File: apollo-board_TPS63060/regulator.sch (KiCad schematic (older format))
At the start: 44 parts, among them J11 Conn_01x04_Male, Q10 2N7002A, Q11 2N7002A, Q13 DMP2035UVT, Q14 DMP2035UVT, Q5 DMP2035UVT, Q9 2N7002A, U10 TPS63060, U9 TPS63060

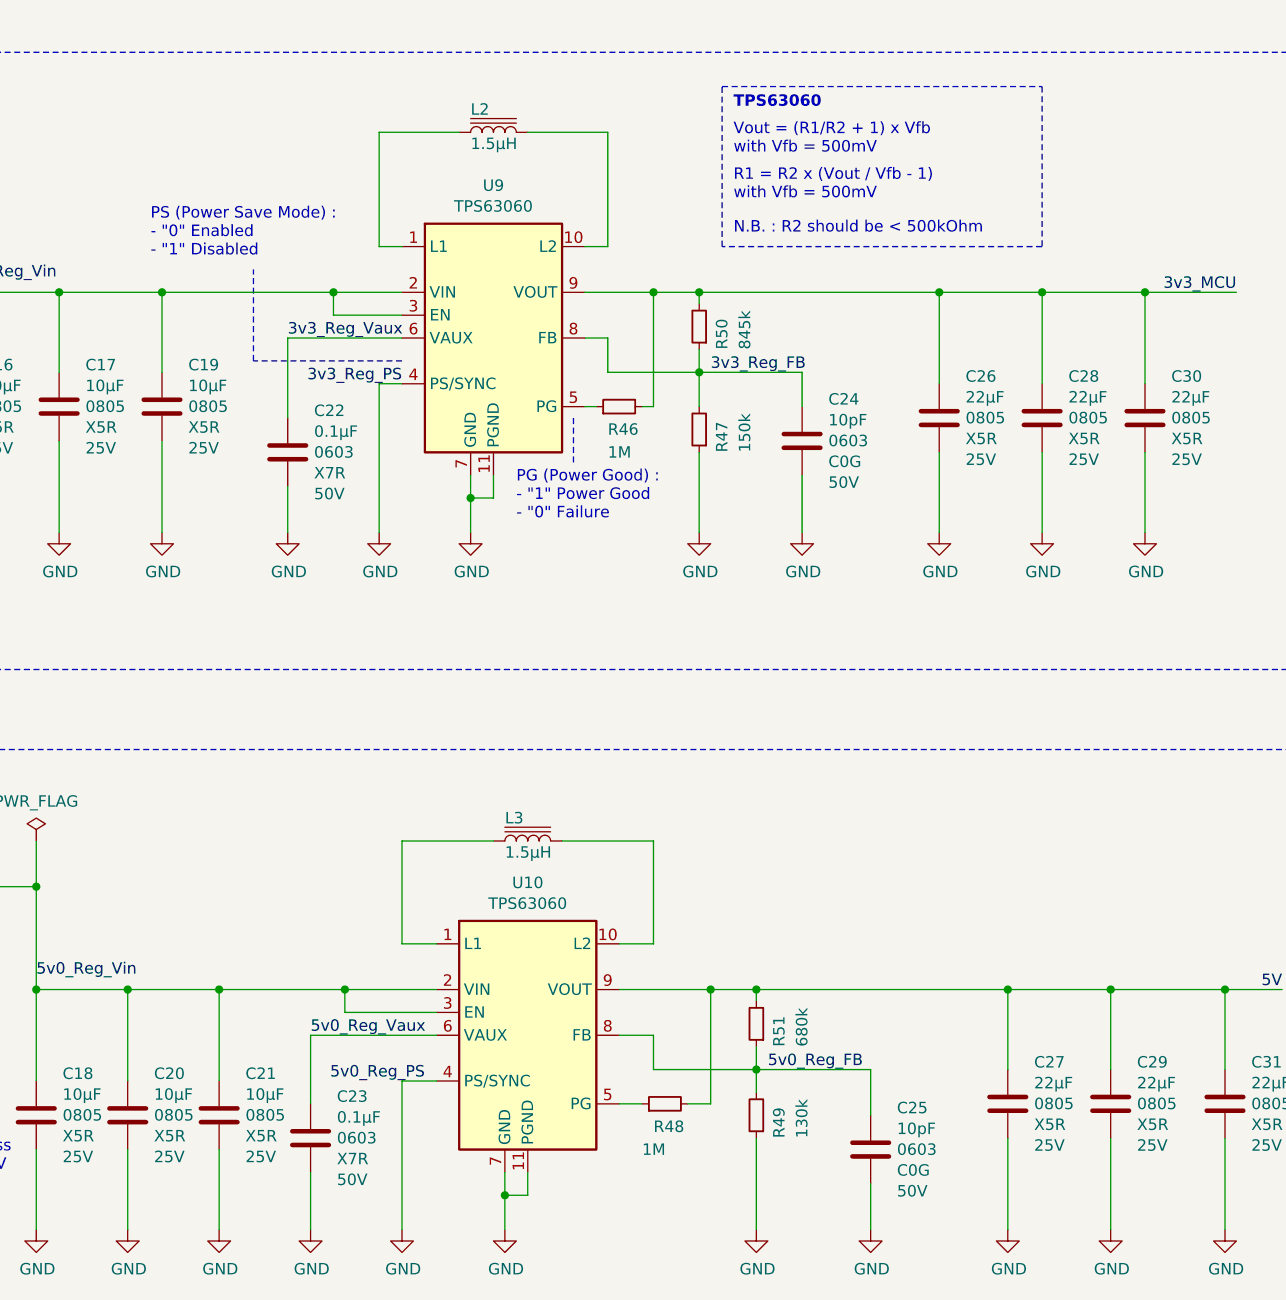
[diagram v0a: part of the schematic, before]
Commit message: Update +5V Buck-Boost Feedback resistor values
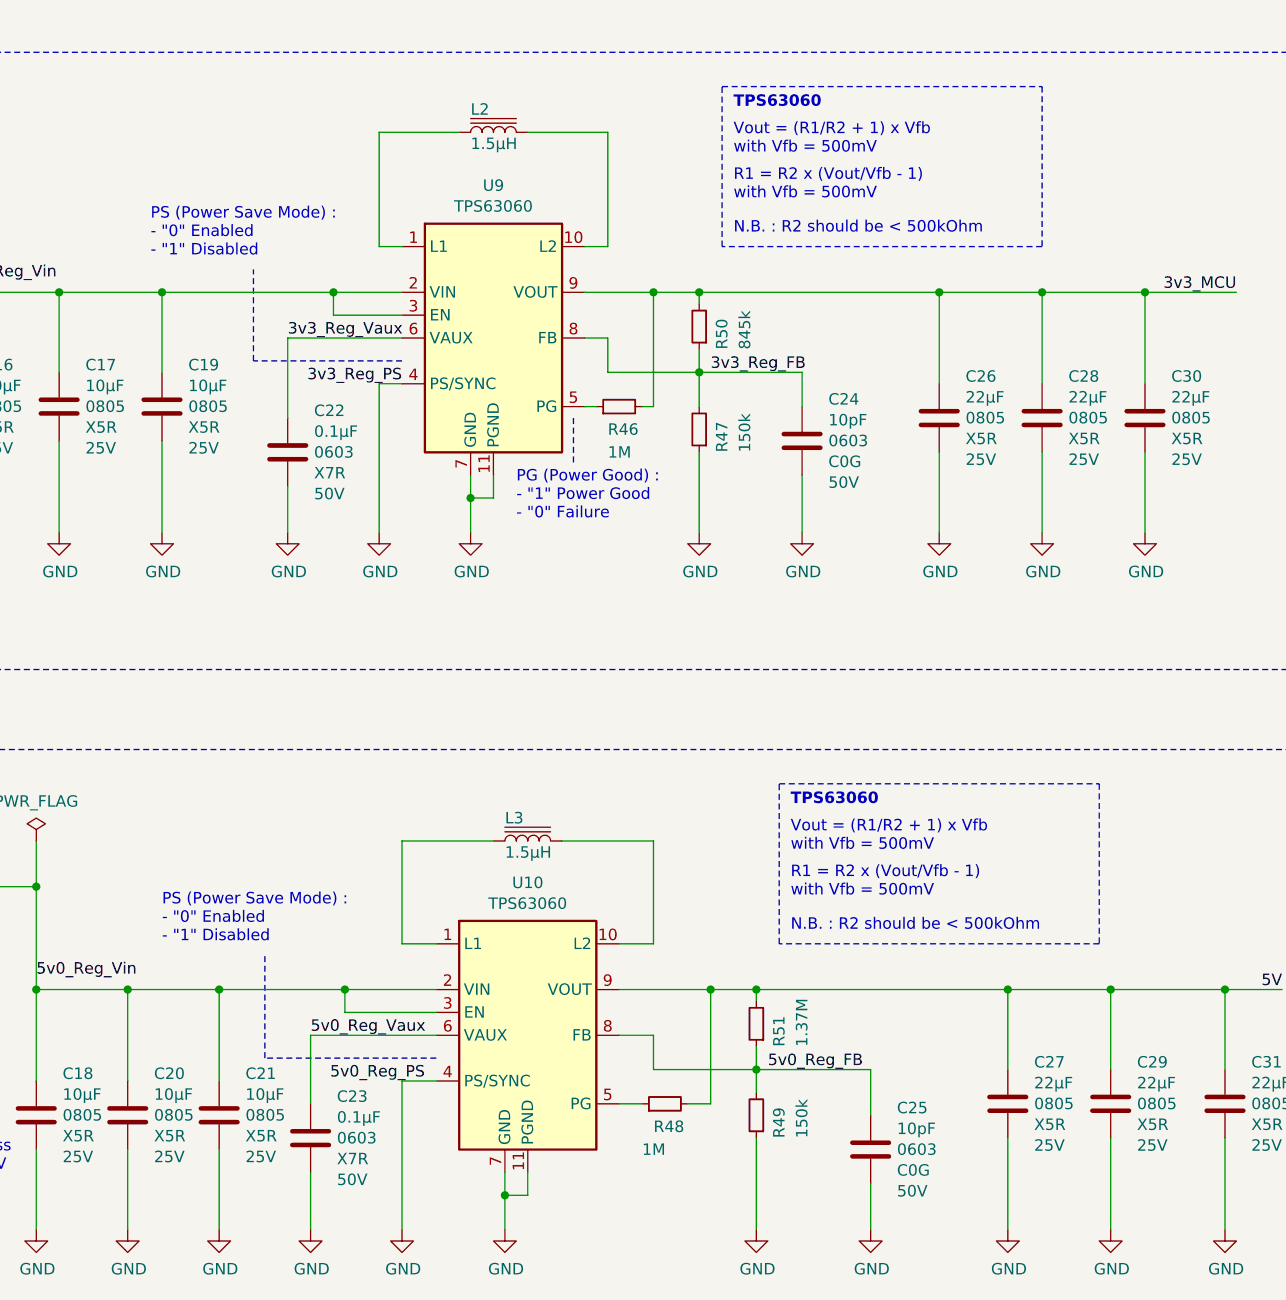
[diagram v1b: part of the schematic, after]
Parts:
- R49: value 130k -> 150k
- R51: value 680k -> 1.37M
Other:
- note added: "R1 = R2 x (Vout/Vfb - 1)\nwith Vfb = 500mV"
- note removed: "R1 = R2 x (Vout / Vfb - 1)\nwith Vfb = 500mV"
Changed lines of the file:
@@
 P 8400 5350
 F 0 "R49" V 8300 5450 50  0000 R CNN
-F 1 "130k" V 8200 5450 50  0000 R CNN
+F 1 "150k" V 8200 5450 50  0000 R CNN
 F 2 "Resistor_SMD:R_0603_1608Metric" H 8400 5350 50  0001 C CNN
 F 3 "~" H 8400 5350 50  0001 C CNN
@@
 P 8400 4950
 F 0 "R51" V 8300 5050 50  0000 R CNN
-F 1 "680k" V 8200 5050 50  0000 R CNN
+F 1 "1.37M" V 8200 5050 50  0000 R CNN
 F 2 "Resistor_SMD:R_0603_1608Metric" H 8400 4950 50  0001 C CNN
 F 3 "~" H 8400 4950 50  0001 C CNN
@@
 N.B. : R2 should be < 500kOhm
 Text Notes 8300 1350 0    50   ~ 0
-R1 = R2 x (Vout / Vfb - 1)\nwith Vfb = 500mV
+R1 = R2 x (Vout/Vfb - 1)\nwith Vfb = 500mV
 Wire Notes Line
 	6850 2050 6200 2050
@@
 Wire Wire Line
 	5250 4800 5250 5200
+Text Notes 8550 4200 0    50   ~ 0
+Vout = (R1/R2 + 1) x Vfb\nwith Vfb = 500mV
+Text Notes 8550 4550 0    50   ~ 0
+N.B. : R2 should be < 500kOhm
+Text Notes 8550 4400 0    50   ~ 0
+R1 = R2 x (Vout/Vfb - 1)\nwith Vfb = 500mV
+Text Notes 8550 4000 0    50   ~ 10
+TPS63060
+Wire Notes Line
+	8500 3900 9900 3900
+Wire Notes Line
+	9900 3900 9900 4600
+Wire Notes Line
+	9900 4600 8500 4600
+Wire Notes Line
+	8500 4600 8500 3900
+Text Notes 5800 4600 0    50   ~ 0
+PS (Power Save Mode) :\n- "0" Enabled\n- "1" Disabled
+Wire Notes Line
+	6250 5100 6250 4650
+Wire Notes Line
+	7000 5100 6250 5100
 $EndSCHEMATC

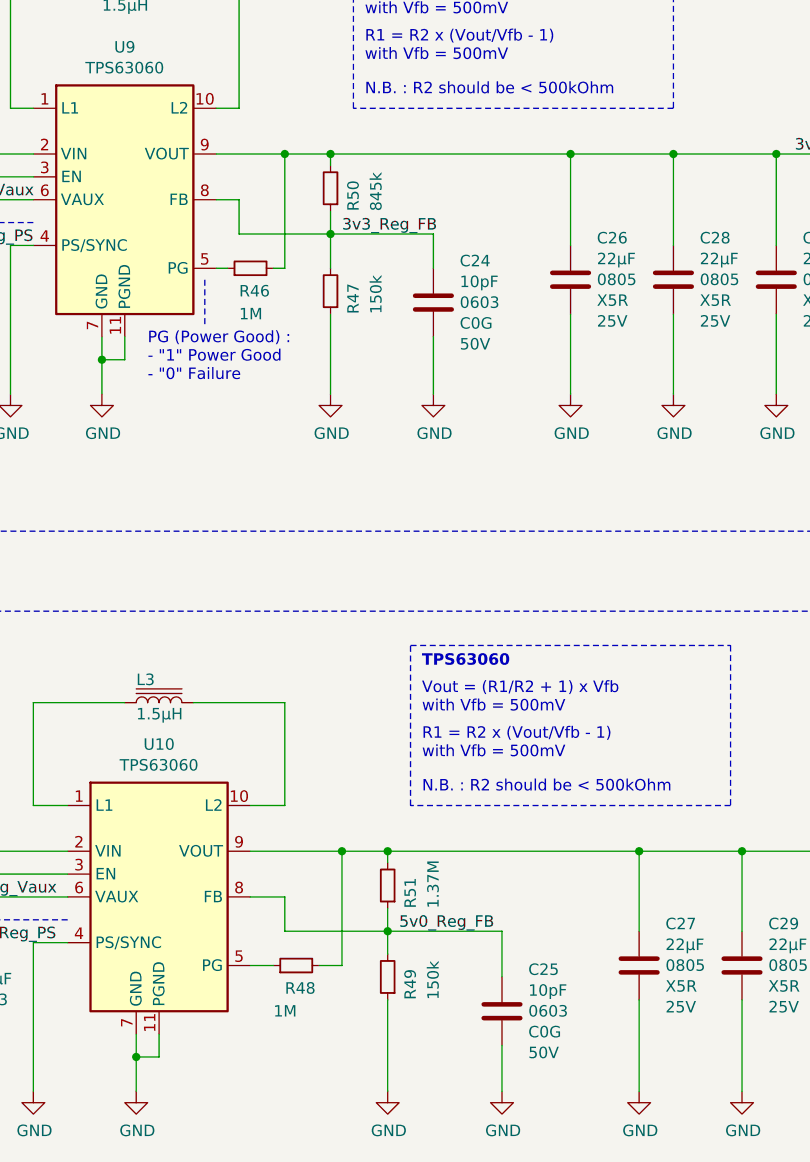
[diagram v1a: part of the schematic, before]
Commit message: Update Buck-Boost Feedback Resistor values
- Use common values + bridge divider iq >3µA
- Misc. Routing : increase one track width from 0.25 to 0.28mm (+5V Output)
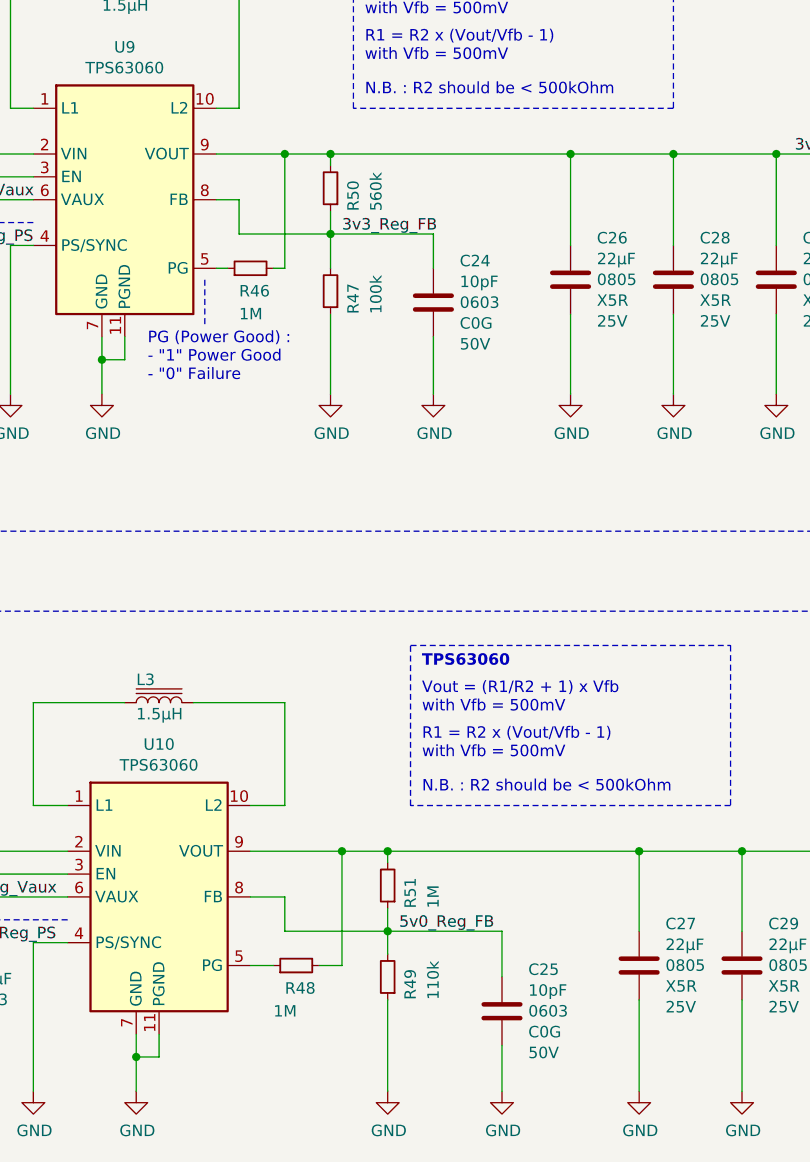
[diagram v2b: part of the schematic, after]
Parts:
- R47: value 150k -> 100k
- R49: value 150k -> 110k
- R50: value 845k -> 560k
- R51: value 1.37M -> 1M
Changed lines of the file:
@@
 P 8400 5350
 F 0 "R49" V 8300 5450 50  0000 R CNN
-F 1 "150k" V 8200 5450 50  0000 R CNN
+F 1 "110k" V 8200 5450 50  0000 R CNN
 F 2 "Resistor_SMD:R_0603_1608Metric" H 8400 5350 50  0001 C CNN
 F 3 "~" H 8400 5350 50  0001 C CNN
@@
 P 8400 4950
 F 0 "R51" V 8300 5050 50  0000 R CNN
-F 1 "1.37M" V 8200 5050 50  0000 R CNN
+F 1 "1M" V 8200 5050 50  0000 R CNN
 F 2 "Resistor_SMD:R_0603_1608Metric" H 8400 4950 50  0001 C CNN
 F 3 "~" H 8400 4950 50  0001 C CNN
@@
 P 8150 1900
 F 0 "R50" V 8050 2000 50  0000 R CNN
-F 1 "845k" V 7950 2000 50  0000 R CNN
+F 1 "560k" V 7950 2000 50  0000 R CNN
 F 2 "Resistor_SMD:R_0603_1608Metric" H 8150 1900 50  0001 C CNN
 F 3 "~" H 8150 1900 50  0001 C CNN
@@
 P 8150 2350
 F 0 "R47" V 8050 2450 50  0000 R CNN
-F 1 "150k" V 7950 2450 50  0000 R CNN
+F 1 "100k" V 7950 2450 50  0000 R CNN
 F 2 "Resistor_SMD:R_0603_1608Metric" H 8150 2350 50  0001 C CNN
 F 3 "~" H 8150 2350 50  0001 C CNN

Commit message: Update USB-C receptacle symbol fields
Add Mfr Name & ref., DataSheet + Alternative Equivalent Part
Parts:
- U10, U9: footprint TPS63060:Texas_S-PWSON-N10_ThermalVias -> TPS63060:Texas_S-PWSON-N10_ThermalVias_NSM_vias_bottom
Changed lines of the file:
@@
 F 0 "U9" H 7250 2617 50  0000 C CNN
 F 1 "TPS63060" H 7250 2526 50  0000 C CNN
-F 2 "TPS63060:Texas_S-PWSON-N10_ThermalVias" H 7250 1300 50  0001 C CNN
+F 2 "TPS63060:Texas_S-PWSON-N10_ThermalVias_NSM_vias_bottom" H 7250 1300 50  0001 C CNN
 F 3 "http://www.ti.com/lit/ds/symlink/tps63060.pdf" H 7250 1950 50  0001 C CNN
 	1    7250 1950
@@
 F 0 "U10" H 7400 5667 50  0000 C CNN
 F 1 "TPS63060" H 7400 5576 50  0000 C CNN
-F 2 "TPS63060:Texas_S-PWSON-N10_ThermalVias" H 7400 4350 50  0001 C CNN
+F 2 "TPS63060:Texas_S-PWSON-N10_ThermalVias_NSM_vias_bottom" H 7400 4350 50  0001 C CNN
 F 3 "http://www.ti.com/lit/ds/symlink/tps63060.pdf" H 7400 5000 50  0001 C CNN
 	1    7400 5000

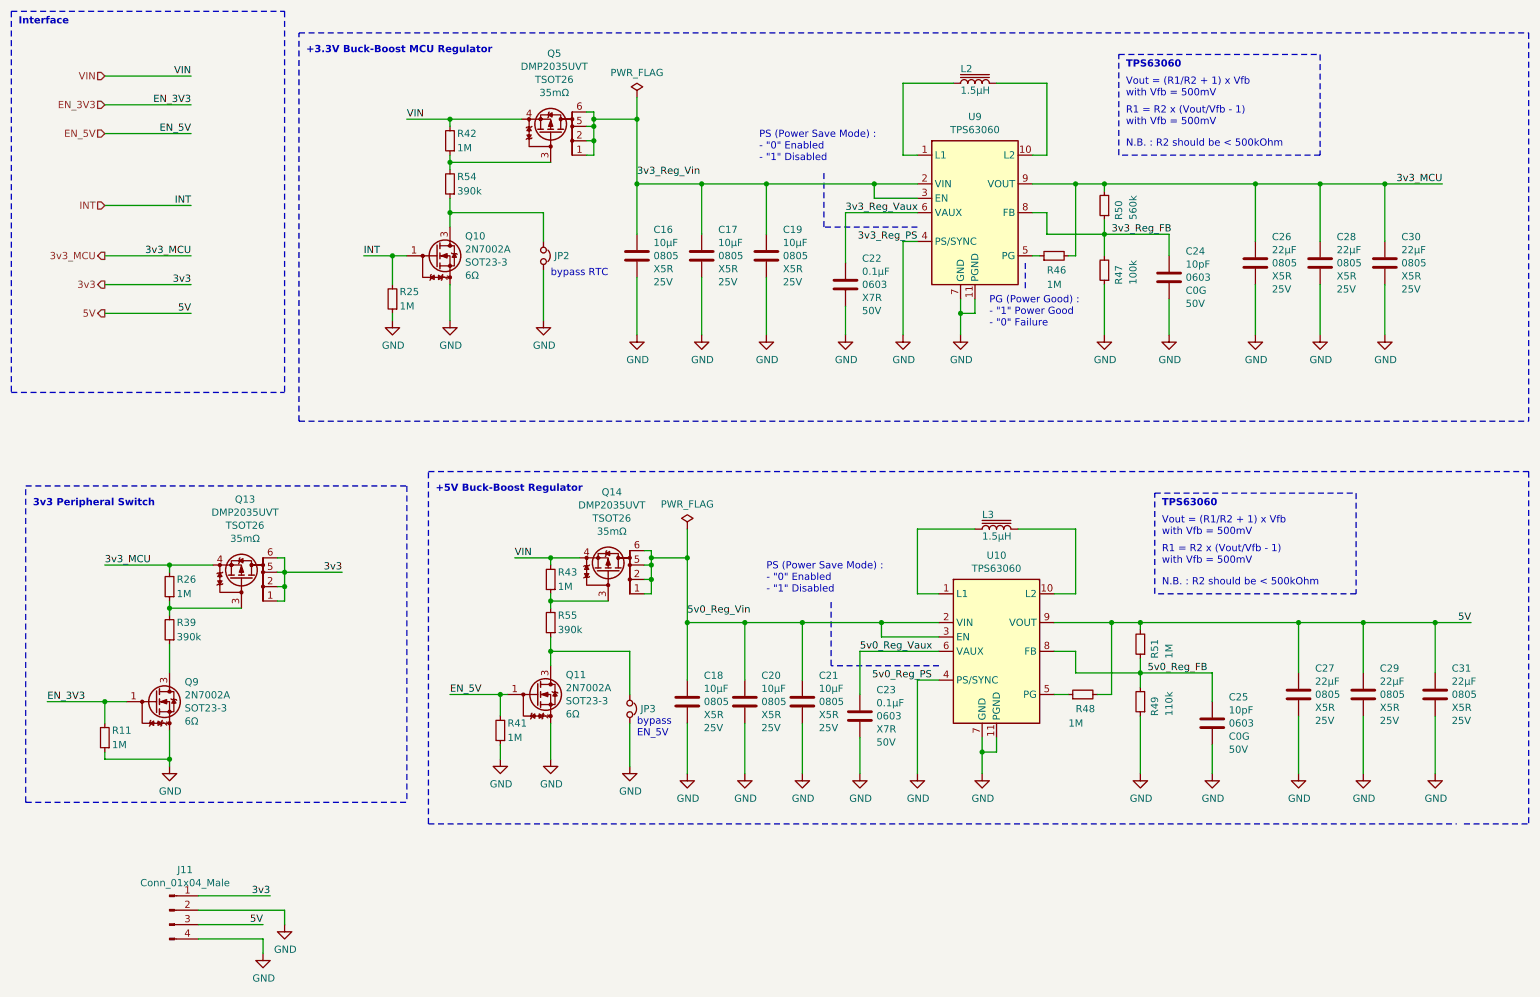
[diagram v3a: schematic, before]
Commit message: Recreate TPS709 symbol to and set footprint to SOT23-5
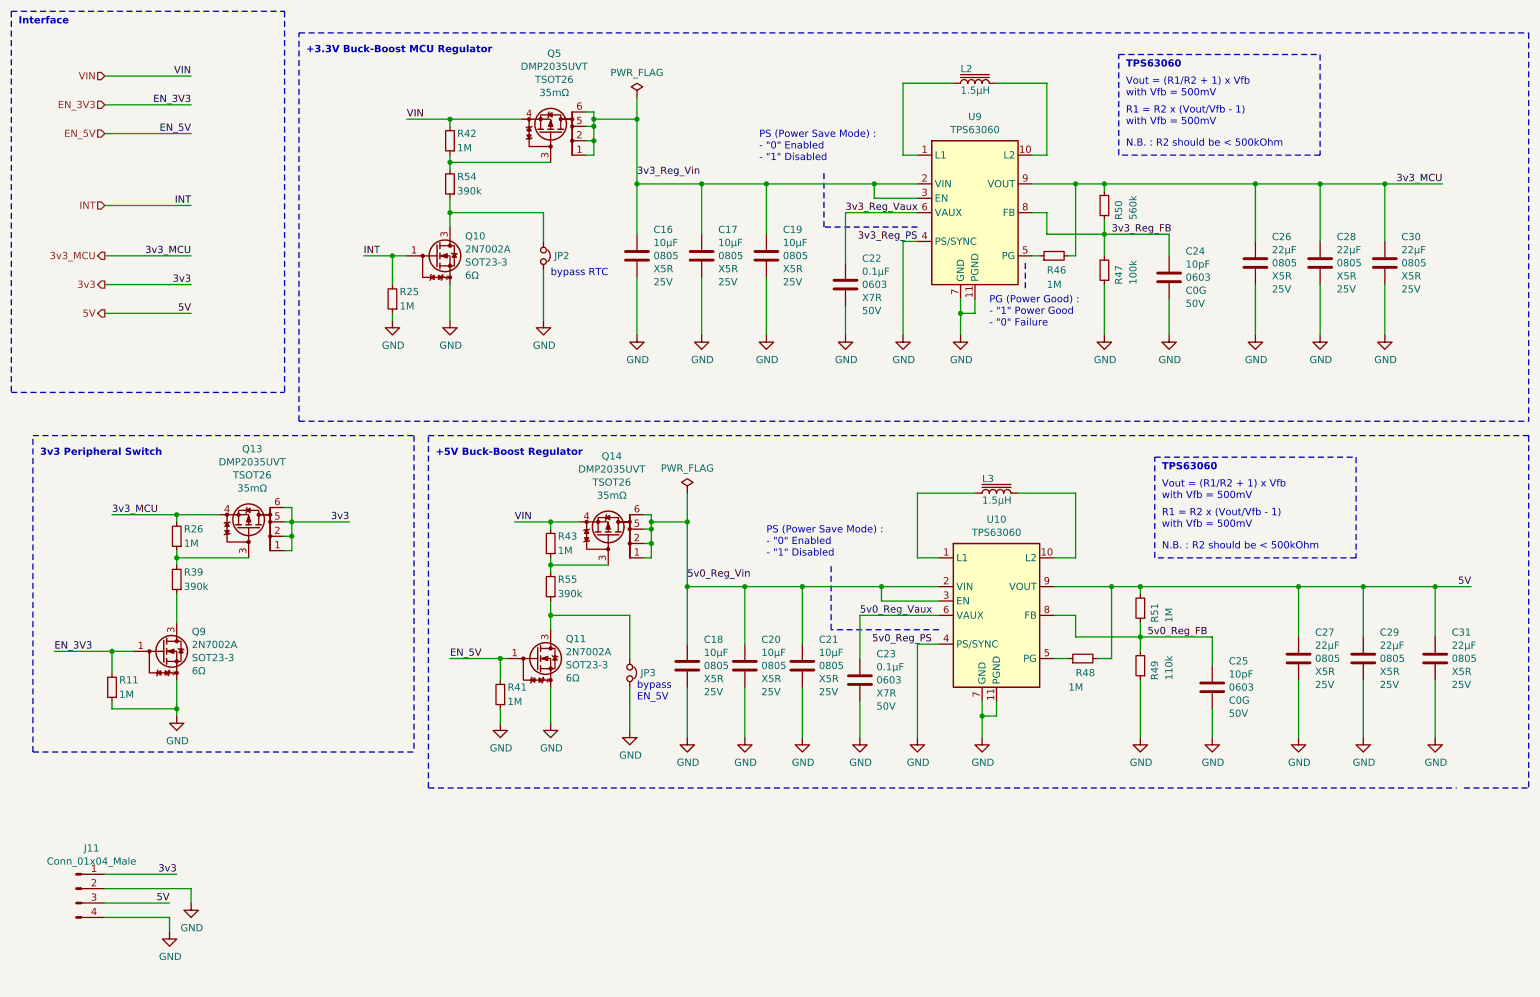
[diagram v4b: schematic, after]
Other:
- moved on the sheet: C18, C20, C21, C23, C25, C27, C29, C31, J11, JP3, L3, Q11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

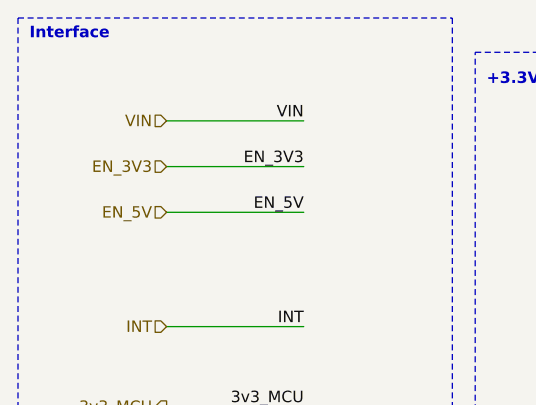
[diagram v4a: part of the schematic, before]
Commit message: Rename some power signal on Schematic to improve readability.
+ Misc. updates
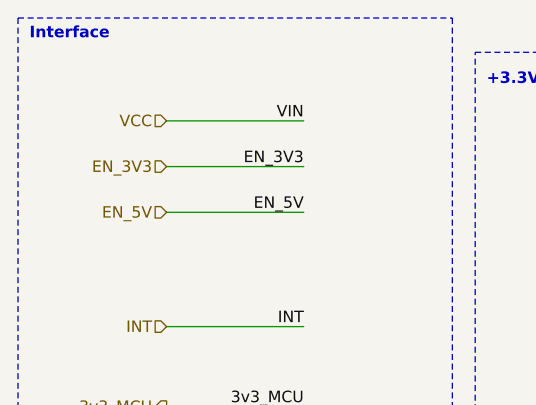
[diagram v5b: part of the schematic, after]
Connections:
- net VIN renamed VCC
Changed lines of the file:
@@
 VIN
 Text HLabel 1200 1000 0    50   Input ~ 0
-VIN
+VCC
 Text Notes 600  650  0    50   ~ 10
 Interface
